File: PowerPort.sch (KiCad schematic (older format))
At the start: 70 parts

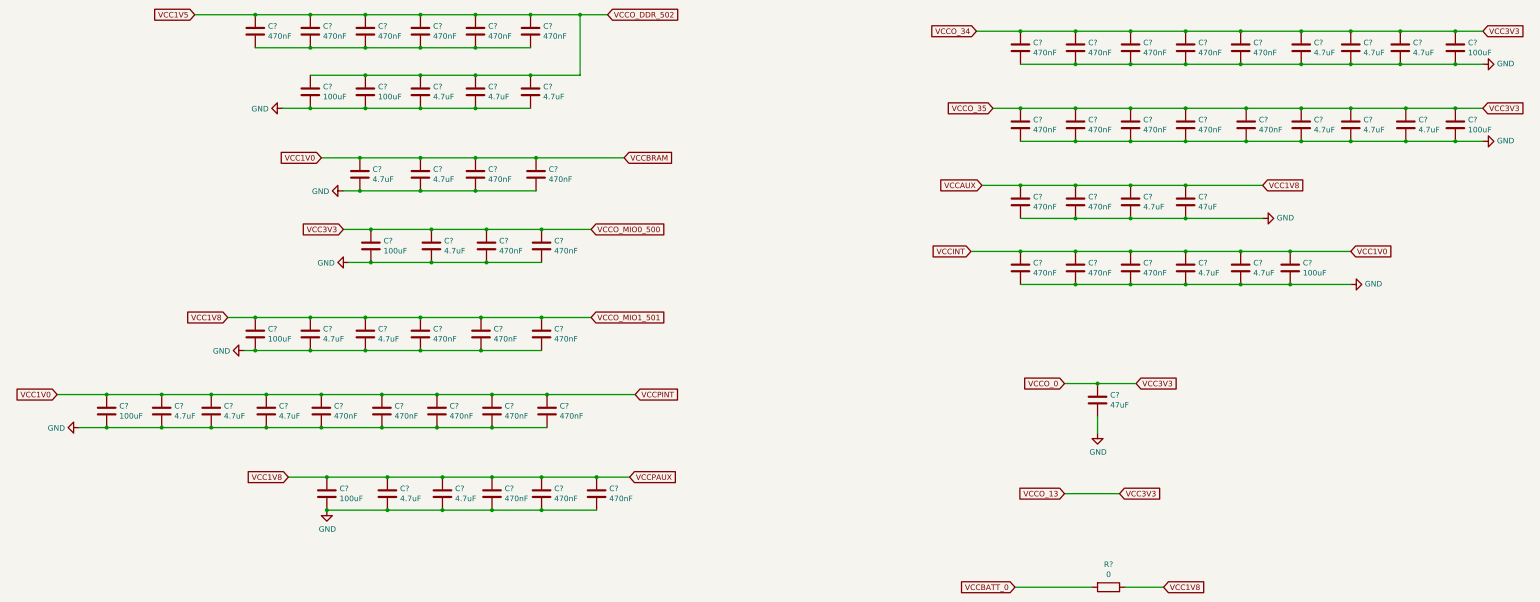
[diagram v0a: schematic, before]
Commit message: add some pmic library
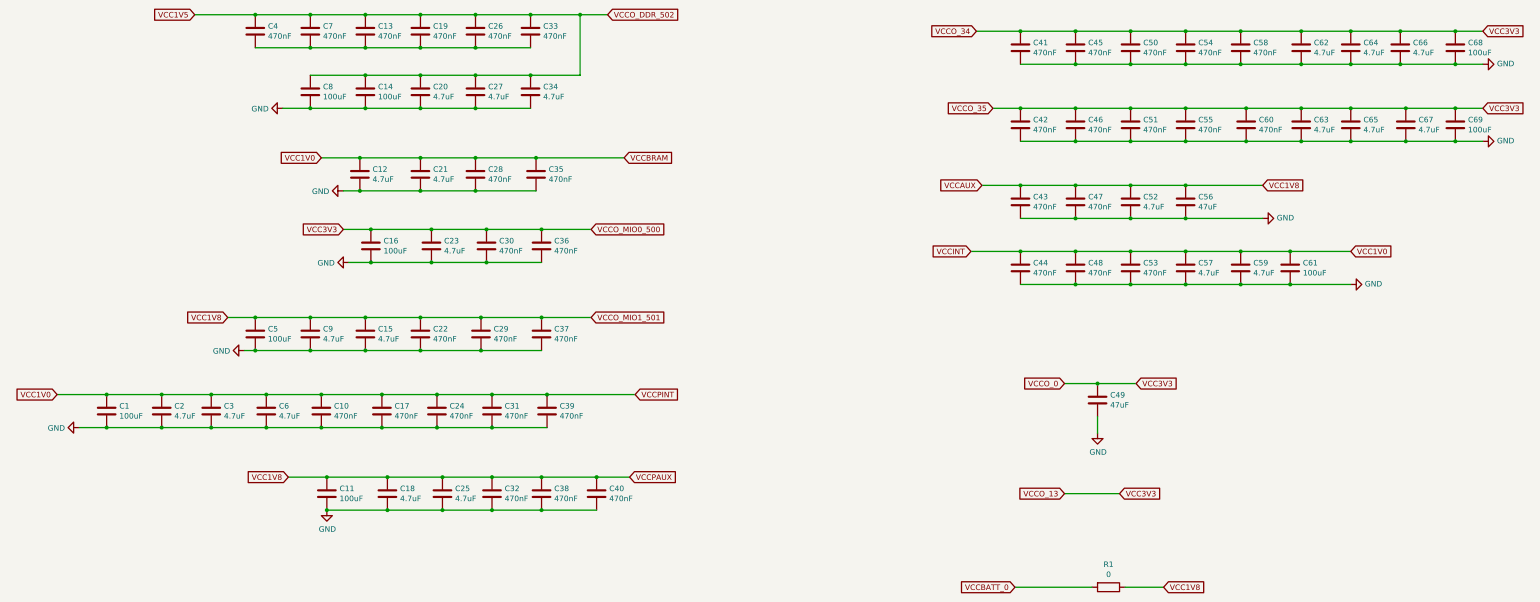
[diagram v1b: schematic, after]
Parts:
- gave numbers to parts that had none: 70
